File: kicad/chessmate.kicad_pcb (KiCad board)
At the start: 2 copper layers, 70 x 125.5 mm, 44 parts, among them J2 Power Jack, Q1 2N2222, Q2 2N2222, Q3 2N2222, Q4 2N2222, Q5 2N2222, SW1 F6, SW10 ENTER, SW11 CLEAR, SW12 H8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

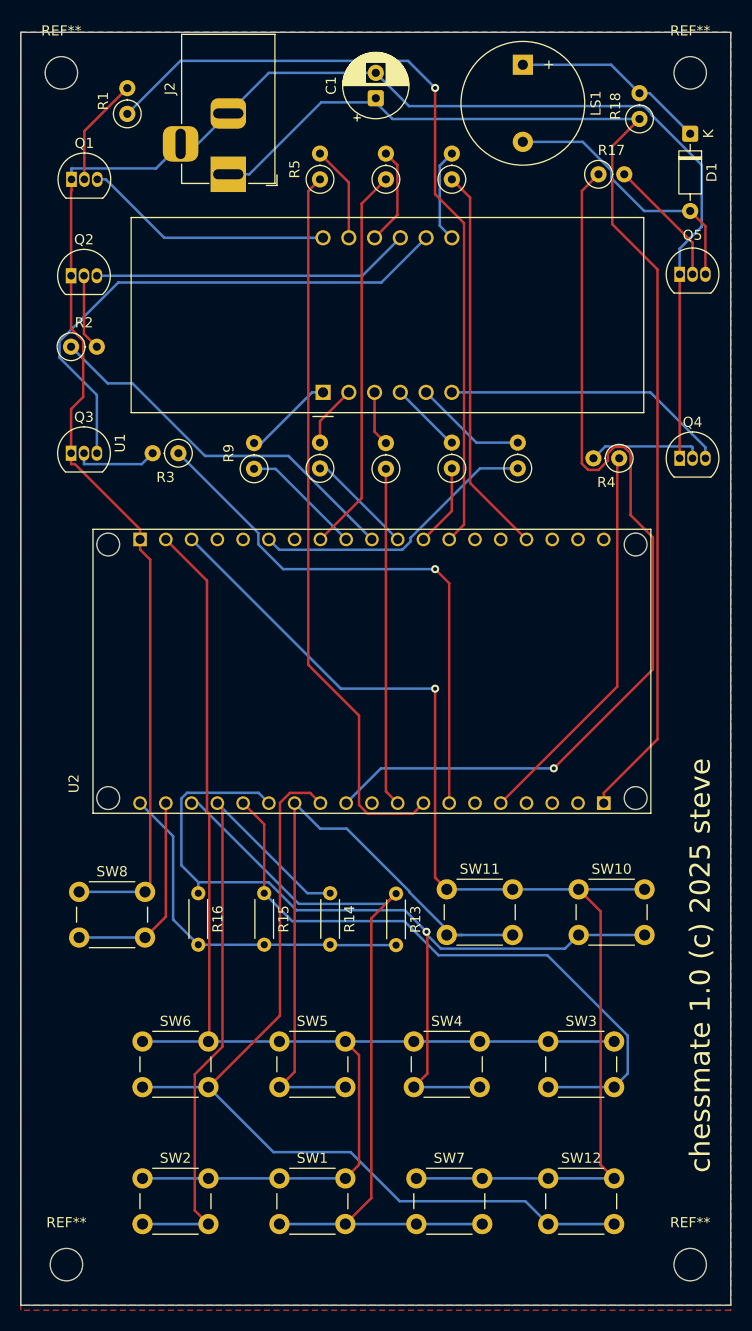
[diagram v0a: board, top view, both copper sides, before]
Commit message: Address v1.0 PCB errors (#13)
* replace 7-seg footprint with pin headers
* update nodemcu footprint
* move component values and switch names to F.Silkscreen layer
* routing
* add ground plane
* add mounting holes
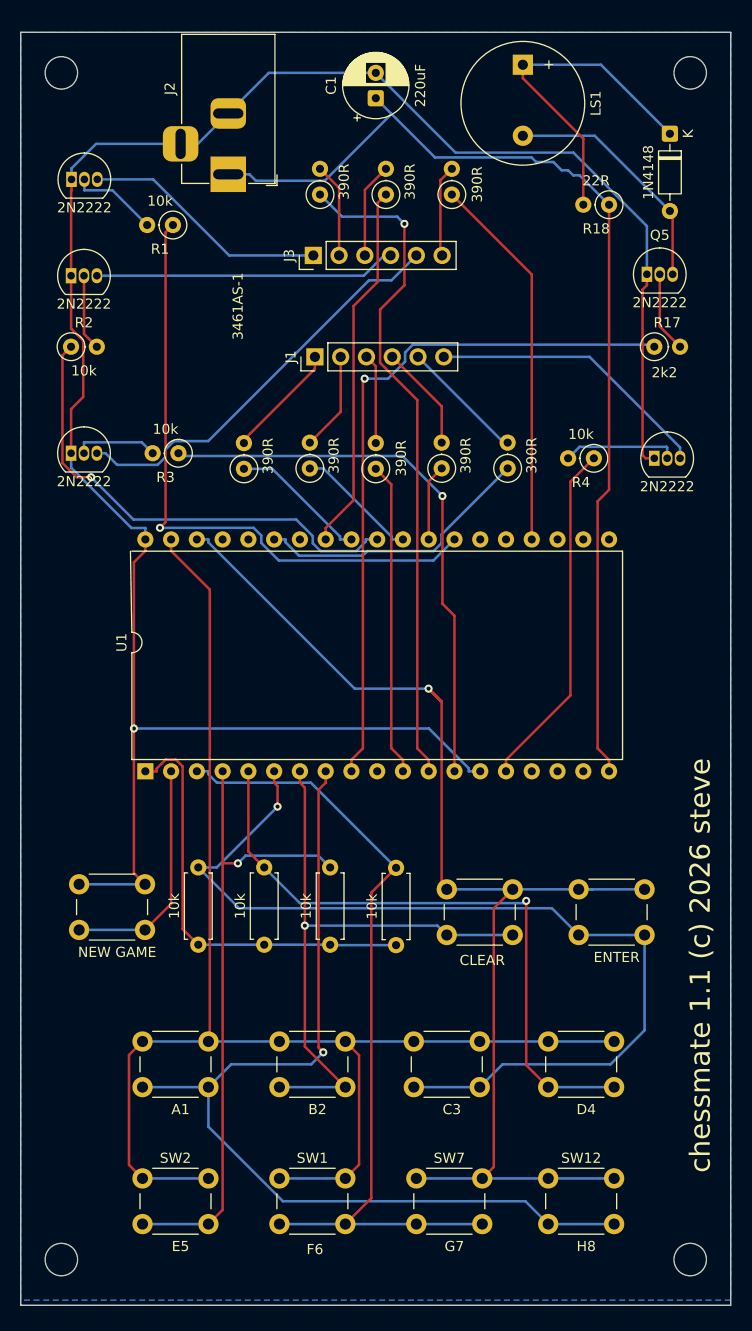
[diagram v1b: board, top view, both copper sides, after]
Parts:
- removed the REF** at (116.0, 140.5)
- removed the REF** at (54.5, 140.5)
- removed U2: ESP32_NODEMCU, esp32-nodemcu:ESP32_NODEMCU
- added J1: 7SegBtm, Connector_PinHeader_2.54mm:PinHeader_1x06_P2.54mm_Vertical, F.Cu at (79.0, 51.0)
- added J3: 7SegTop, Connector_PinHeader_2.54mm:PinHeader_1x06_P2.54mm_Vertical, F.Cu at (78.8, 41.0)
- added REF**: MountingHole_3.2mm_M3, MountingHole:MountingHole_3.2mm_M3, F.Cu at (54.0, 140.0)
- added REF**: MountingHole_3.2mm_M3, MountingHole:MountingHole_3.2mm_M3, F.Cu at (116.0, 140.0)
- LS1: footprint Buzzer_Beeper:Buzzer_12x9.5RM7.6 -> stevelib:Buzzer_12x9.5RM7.0
- R13, R14, R15, R16: footprint Resistor_THT:R_Axial_DIN0204_L3.6mm_D1.6mm_P5.08mm_Horizontal -> Resistor_THT:R_Axial_DIN0207_L6.3mm_D2.5mm_P7.62mm_Horizontal
- U1: value CC56-12SURKWA -> AI-Thinker Nodemcu-32S; footprint Display_7Segment:CA56-12SURKWA -> kicad-nodemcu32S-main:ai-thinker nodemcu-32s
- moved U1 41.3 mm to (62.3, 91.9)
- moved R17 17.9 mm to (112.5, 50.0)
- moved R1 11.8 mm to (65.0, 38.0), turned to 180 degrees
- moved R18 8.97 mm to (108.0, 36.0), turned to 180 degrees
- moved Q5 3.23 mm to (111.7, 42.9)
- moved R13 2.54 mm to (87.0, 101.4)
- moved R14 2.54 mm to (80.5, 101.3)
- moved R15 2.54 mm to (74.0, 101.3)
- moved R16 2.54 mm to (67.5, 101.3)
- moved Q4 2.50 mm to (112.5, 61.0)
- moved R4 2.50 mm to (106.5, 61.0)
- moved D1 2.00 mm to (114.0, 29.0)
- moved R10 1.50 mm to (86.0, 35.0)
- moved R5 1.50 mm to (79.5, 35.0)
- moved R6 1.50 mm to (92.5, 35.0)
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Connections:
- Q1 pad 3: /DIG1 -> D1
- Q2 pad 3: /DIG2 -> D2
- Q3 pad 3: /DIG3 -> D3
- Q4 pad 3: /DIG4 -> D4
- R10 pad 2: Net-(U1-f) -> F
- R11 pad 2: Net-(U1-g) -> G
- R12 pad 2: Net-(U1-DPX) -> DP
- R5 pad 2: Net-(U1-a) -> A
- R6 pad 2: Net-(U1-b) -> B
- R7 pad 2: Net-(U1-c) -> C
- R8 pad 2: Net-(U1-d) -> D
- R9 pad 2: Net-(U1-e) -> E
- U1 pad 1: Net-(U1-e) -> +3V3
- U1 pad 10: Net-(U1-f) -> unconnected-(U1-GPIO26-Pad10)
- U1 pad 11: Net-(U1-a) -> /DP_PIN
- U1 pad 12: /DIG1 -> /SEGA_PIN
- U1 pad 2: Net-(U1-d) -> /RESET_PIN
- U1 pad 3: Net-(U1-DPX) -> /COL0_PIN
- U1 pad 4: Net-(U1-c) -> /COL1_PIN
- U1 pad 5: Net-(U1-g) -> /COL2_PIN
- U1 pad 6: /DIG4 -> /COL3_PIN
- U1 pad 7: Net-(U1-b) -> /COL4_PIN
- U1 pad 8: /DIG3 -> /COL5_PIN
- U1 pad 9: /DIG2 -> /SOUND_PIN
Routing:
- net /DIG3: track 52.9 -> 0.00 mm
- net D3: track 0.00 -> 41.0 mm
- net /DIG2: track 31.5 -> 0.00 mm
- net D2: track 0.00 -> 29.8 mm
- net /DIG4: track 28.3 -> 0.00 mm
- net D4: track 0.00 -> 28.1 mm
- net GND: track 182.2 -> 210.0 mm, vias 0 -> 1
- net /DIG1: track 24.6 -> 0.00 mm
- net D1: track 0.00 -> 24.4 mm
- net /SOUND_PIN: track 93.8 -> 69.8 mm
- net /DIG1_PIN: track 79.9 -> 62.5 mm
- net Net-(D1-K): track 19.3 -> 33.6 mm
- net +5V: track 117.2 -> 103.2 mm
- net G: track 0.00 -> 12.3 mm
- net E: track 0.00 -> 11.4 mm
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- removed copper zone on F.Cu, net +3V3
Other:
- board text added: "3461AS-1"
- board text added: "chessmate 1.1 (c) 2026 steve"
- board text removed: "chessmate 1.0 (c) 2025 steve"
